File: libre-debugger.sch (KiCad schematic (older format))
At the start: 76 parts, among them J1 USB_C_Receptacle_USB2.0, J2 Conn_ST_STDC14, J4 Conn_01x10, Q1 2N7002, SW1 SW_SPDT, SW2 SW_Push, U1 FT2232H, U10 74LVC1G125, U11 74LVC1G125, U12 74LVC1G125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

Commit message: Progress placement.
Most components placed.
Most routing pending.
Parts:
- added LOGO1: Logo_Open_Hardware_Small, Symbol:OSHW-Logo_5.7x6mm_SilkScreen, symbol Graphic:Logo_Open_Hardware_Small
- J4: value Conn_01x10 -> Conn_01x14; footprint Connector_PinHeader_2.54mm:PinHeader_1x10_P2.54mm_Vertical -> Connector_PinHeader_2.54mm:PinHeader_1x14_P2.54mm_Vertical; symbol Connector_Generic:Conn_01x10 -> Connector_Generic:Conn_01x14
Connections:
- net labels added: GPIO0, GPIO1, GPIO2, GPIO3
- wire segments 338 -> 346
- no-connect marks 22 -> 18
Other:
- note added: "CAP on VREGIN?"
- moved on the sheet: D1, R7
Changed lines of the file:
@@
 EESchema Schematic File Version 5
-LIBS:libre-debugger-cache
 EELAYER 30 0
 EELAYER END
@@
 Comment3 ""
 Comment4 ""
+Comment5 ""
+Comment6 ""
+Comment7 ""
+Comment8 ""
+Comment9 ""
 $EndDescr
 Text Label 5650 5150 0    50   ~ 0
@@
 $EndComp
 $Comp
-L Graphic:Logo_Open_Hardware_Small #LOGO1
+L Graphic:Logo_Open_Hardware_Small LOGO1
 U 1 1 5C96BFCB
 P 15550 10250
-F 0 "#LOGO1" H 15550 10525 50  0001 C CNN
+F 0 "LOGO1" H 15550 10525 50  0001 C CNN
 F 1 "Logo_Open_Hardware_Small" H 15550 10025 50  0001 C CNN
-F 2 "" H 15550 10250 50  0001 C CNN
+F 2 "Symbol:OSHW-Logo_5.7x6mm_SilkScreen" H 15550 10250 50  0001 C CNN
 F 3 "~" H 15550 10250 50  0001 C CNN
 	1    15550 10250
@@
 L Device:LED D1
 U 1 1 5C62F385
-P 8900 5300
-F 0 "D1" V 8950 5150 50  0000 C CNN
-F 1 "LED" V 8850 5150 50  0000 C CNN
-F 2 "LED_SMD:LED_0603_1608Metric" H 8900 5300 50  0001 C CNN
-F 3 "~" H 8900 5300 50  0001 C CNN
-	1    8900 5300
+P 9200 5300
+F 0 "D1" V 9250 5150 50  0000 C CNN
+F 1 "LED" V 9150 5150 50  0000 C CNN
+F 2 "LED_SMD:LED_0603_1608Metric" H 9200 5300 50  0001 C CNN
+F 3 "~" H 9200 5300 50  0001 C CNN
+	1    9200 5300
 	0    -1   -1   0
 $EndComp
-Text Label 8900 5150 0    50   ~ 0
+Text Label 9200 5150 0    50   ~ 0
 MPSSE_LED_A
 Wire Wire Line
-	8400 4750 8900 4750
+	8400 4750 9200 4750
 $Comp
 L power:GND #PWR031
 U 1 1 5C6507DD
-P 8900 5500
-F 0 "#PWR031" H 8900 5250 50  0001 C CNN
-F 1 "GND" H 8905 5327 50  0000 C CNN
-F 2 "" H 8900 5500 50  0001 C CNN
-F 3 "" H 8900 5500 50  0001 C CNN
-	1    8900 5500
+P 9200 5500
+F 0 "#PWR031" H 9200 5250 50  0001 C CNN
+F 1 "GND" H 9205 5327 50  0000 C CNN
+F 2 "" H 9200 5500 50  0001 C CNN
+F 3 "" H 9200 5500 50  0001 C CNN
+	1    9200 5500
 	1    0    0    -1
 $EndComp
@@
 L Device:R R7
 U 1 1 5C62F38F
-P 8900 4900
-F 0 "R7" H 8800 4850 50  0000 C CNN
-F 1 "470R" H 8750 4950 50  0000 C CNN
-F 2 "Resistor_SMD:R_0603_1608Metric" V 8830 4900 50  0001 C CNN
-F 3 "~" H 8900 4900 50  0001 C CNN
-	1    8900 4900
+P 9200 4900
+F 0 "R7" H 9100 4850 50  0000 C CNN
+F 1 "470R" H 9050 4950 50  0000 C CNN
+F 2 "Resistor_SMD:R_0603_1608Metric" V 9130 4900 50  0001 C CNN
+F 3 "~" H 9200 4900 50  0001 C CNN
+	1    9200 4900
 	-1   0    0    1
 $EndComp
 Wire Wire Line
-	8900 5500 8900 5450
-Wire Wire Line
-	8900 5150 8900 5050
+	9200 5500 9200 5450
+Wire Wire Line
+	9200 5150 9200 5050
 Wire Wire Line
 	8400 4350 9950 4350
@@
 NoConn ~ 8400 5450
 NoConn ~ 8400 5350
-NoConn ~ 8400 5250
-NoConn ~ 8400 5150
-NoConn ~ 8400 5050
-NoConn ~ 8400 4950
 NoConn ~ 8400 7750
 $Comp
@@
 Text Label 5650 5350 0    50   ~ 0
 REF
-Wire Wire Line
-	15450 6400 14700 6400
-Wire Wire Line
-	15450 6600 14700 6600
-Wire Wire Line
-	14700 6500 15450 6500
-Wire Wire Line
-	14700 6700 15450 6700
-Wire Wire Line
-	14700 6300 15450 6300
 Text Label 14900 6400 0    50   ~ 0
 TCK_TRGT
@@
 L power:GND #PWR0105
 U 1 1 5CB1DC59
-P 15350 7050
-F 0 "#PWR0105" H 15350 6800 50  0001 C CNN
-F 1 "GND" H 15355 6877 50  0000 C CNN
-F 2 "" H 15350 7050 50  0001 C CNN
-F 3 "" H 15350 7050 50  0001 C CNN
-	1    15350 7050
-	1    0    0    -1
-$EndComp
-Wire Wire Line
-	15350 7050 15350 7000
-Wire Wire Line
-	15350 7000 15450 7000
-Wire Wire Line
-	15000 6200 15450 6200
-Wire Wire Line
-	15250 6100 15450 6100
+P 14850 7050
+F 0 "#PWR0105" H 14850 6800 50  0001 C CNN
+F 1 "GND" H 14855 6877 50  0000 C CNN
+F 2 "" H 14850 7050 50  0001 C CNN
+F 3 "" H 14850 7050 50  0001 C CNN
+	1    14850 7050
+	1    0    0    -1
+$EndComp
 Text Label 12750 1000 0    50   ~ 0
 SRST_N_R
@@
 Connection ~ 9150 3350
 $Comp
-L Connector_Generic:Conn_01x10 J4
-U 1 1 5D592546
-P 15650 6500
-F 0 "J4" H 15600 7000 50  0000 L CNN
-F 1 "Conn_01x10" H 15500 5900 50  0000 L CNN
-F 2 "Connector_PinHeader_2.54mm:PinHeader_1x10_P2.54mm_Vertical" H 15650 6500 50  0001 C CNN
-F 3 "~" H 15650 6500 50  0001 C CNN
-	1    15650 6500
-	1    0    0    -1
-$EndComp
-$Comp
 L Connector:Conn_ST_STDC14 J2
 U 1 1 5D5978D5
@@
 Wire Wire Line
 	15100 3600 14450 3600
-Wire Wire Line
-	15450 6800 14700 6800
-Wire Wire Line
-	15450 6900 14700 6900
 Text Label 14900 6800 0    50   ~ 0
 TXD_TRGT
@@
 	14500 5700 16000 5700
 Wire Notes Line
-	16000 5700 16000 7300
+	16000 5700 16000 7550
 Wire Notes Line
-	16000 7300 14500 7300
+	16000 7550 14500 7550
 Wire Notes Line
-	14500 7300 14500 5700
+	14500 7550 14500 5700
 Text Notes 14550 5800 0    50   ~ 10
 AUX header
@@
 	0    1    1    0
 $EndComp
+Text Notes 5150 4150 0    50   ~ 0
+CAP on VREGIN?
+Wire Wire Line
+	15450 6800 14700 6800
+Wire Wire Line
+	15450 6900 14700 6900
+$Comp
+L Connector_Generic:Conn_01x14 J4
+U 1 1 5D592546
+P 15650 6700
+F 0 "J4" H 15600 7200 50  0000 L CNN
+F 1 "Conn_01x14" H 15400 5900 50  0000 L CNN
+F 2 "Connector_PinHeader_2.54mm:PinHeader_1x14_P2.54mm_Vertical" H 15650 6700 50  0001 C CNN
+F 3 "~" H 15650 6700 50  0001 C CNN
+	1    15650 6700
+	1    0    0    -1
+$EndComp
+Wire Wire Line
+	15250 6100 15450 6100
+Wire Wire Line
+	15000 6200 15450 6200
+Wire Wire Line
+	14700 6300 15450 6300
+Wire Wire Line
+	14700 6700 15450 6700
+Wire Wire Line
+	14700 6500 15450 6500
+Wire Wire Line
+	15450 6400 14700 6400
+Wire Wire Line
+	15450 6600 14700 6600
+Wire Wire Line
+	14850 7000 14850 7050
+Wire Wire Line
+	14850 7000 15450 7000
+Text Label 8450 5250 0    50   ~ 0
+GPIO3
+Text Label 8450 5150 0    50   ~ 0
+GPIO2
+Text Label 8450 5050 0    50   ~ 0
+GPIO1
+Text Label 8450 4950 0    50   ~ 0
+GPIO0
+Wire Wire Line
+	8400 4950 8700 4950
+Wire Wire Line
+	8400 5050 8700 5050
+Wire Wire Line
+	8400 5150 8700 5150
+Wire Wire Line
+	8400 5250 8700 5250
+Text Label 15150 7100 0    50   ~ 0
+GPIO3
+Wire Wire Line
+	15450 7100 15100 7100
+Wire Wire Line
+	15450 7200 15100 7200
+Wire Wire Line
+	15450 7300 15100 7300
+Wire Wire Line
+	15450 7400 15100 7400
+Text Label 15150 7200 0    50   ~ 0
+GPIO2
+Text Label 15150 7300 0    50   ~ 0
+GPIO1
+Text Label 15150 7400 0    50   ~ 0
+GPIO0
 $EndSCHEMATC

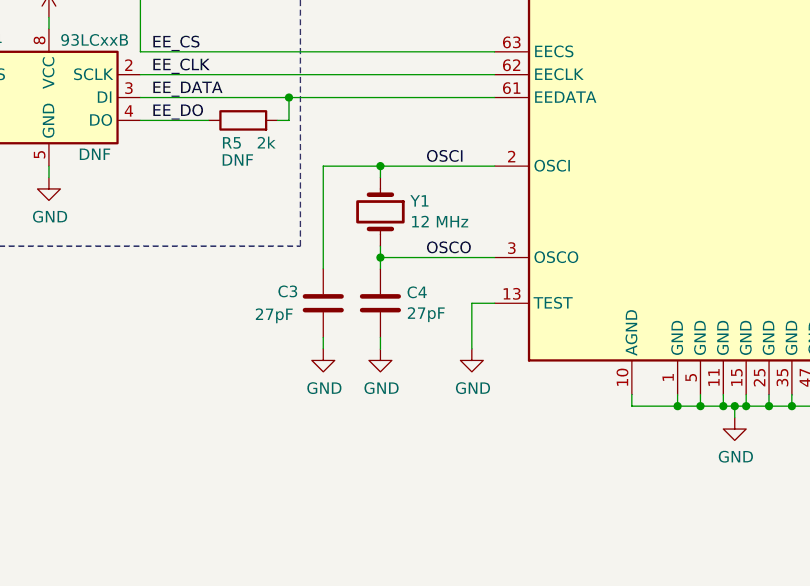
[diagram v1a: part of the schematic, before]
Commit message: SCH: Replace HC49 crystal by 3225
Schematic only. Layout update pending.
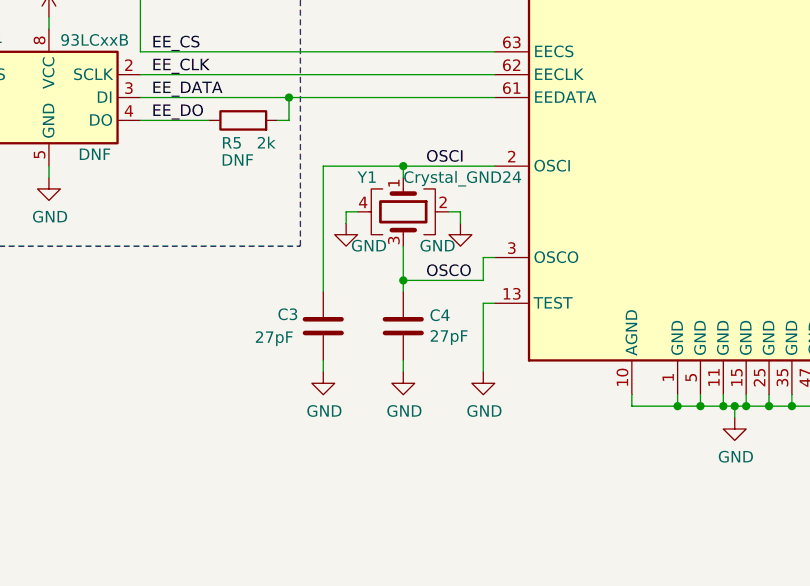
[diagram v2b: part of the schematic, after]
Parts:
- removed Y1: 12 MHz, Crystal:Crystal_SMD_HC49-SD, symbol Device:Crystal
- added Y1: Crystal_GND24, Crystal:Crystal_SMD_3225-4Pin_3.2x2.5mm, symbol Device:Crystal_GND24
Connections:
- wire segments 346 -> 352
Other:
- moved on the sheet: C3, C4
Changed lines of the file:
@@
 Text Label 5650 5050 0    50   ~ 0
 USB_DM
-$Comp
-L Device:Crystal Y1
-U 1 1 5C621971
-P 5500 7350
-F 0 "Y1" V 5454 7481 50  0000 L CNN
-F 1 "12 MHz" V 5545 7481 50  0000 L CNN
-F 2 "Crystal:Crystal_SMD_HC49-SD" H 5500 7350 50  0001 C CNN
-F 3 "~" H 5500 7350 50  0001 C CNN
-	1    5500 7350
-	0    1    1    0
-$EndComp
-Wire Wire Line
-	6000 7550 5500 7550
-Wire Wire Line
-	5500 7550 5500 7500
-Wire Wire Line
-	6000 7150 5500 7150
-Wire Wire Line
-	5500 7150 5500 7200
+Wire Wire Line
+	6000 7550 5950 7550
 $Comp
 L Device:C C4
 U 1 1 5C623C6B
-P 5500 7750
-F 0 "C4" H 5615 7796 50  0000 L CNN
-F 1 "27pF" H 5615 7705 50  0000 L CNN
-F 2 "Capacitor_SMD:C_0603_1608Metric" H 5538 7600 50  0001 C CNN
-F 3 "~" H 5500 7750 50  0001 C CNN
-	1    5500 7750
+P 5600 7850
+F 0 "C4" H 5715 7896 50  0000 L CNN
+F 1 "27pF" H 5715 7805 50  0000 L CNN
+F 2 "Capacitor_SMD:C_0603_1608Metric" H 5638 7700 50  0001 C CNN
+F 3 "~" H 5600 7850 50  0001 C CNN
+	1    5600 7850
 	1    0    0    -1
 $EndComp
@@
 L Device:C C3
 U 1 1 5C6244F4
-P 5250 7750
-F 0 "C3" H 5050 7800 50  0000 L CNN
-F 1 "27pF" H 4950 7700 50  0000 L CNN
-F 2 "Capacitor_SMD:C_0603_1608Metric" H 5288 7600 50  0001 C CNN
-F 3 "~" H 5250 7750 50  0001 C CNN
-	1    5250 7750
+P 5250 7850
+F 0 "C3" H 5050 7900 50  0000 L CNN
+F 1 "27pF" H 4950 7800 50  0000 L CNN
+F 2 "Capacitor_SMD:C_0603_1608Metric" H 5288 7700 50  0001 C CNN
+F 3 "~" H 5250 7850 50  0001 C CNN
+	1    5250 7850
 	1    0    0    -1
 $EndComp
@@
 L power:GND #PWR020
 U 1 1 5C624CB0
-P 5500 7950
-F 0 "#PWR020" H 5500 7700 50  0001 C CNN
-F 1 "GND" H 5505 7777 50  0000 C CNN
-F 2 "" H 5500 7950 50  0001 C CNN
-F 3 "" H 5500 7950 50  0001 C CNN
-	1    5500 7950
-	1    0    0    -1
-$EndComp
-Wire Wire Line
-	5500 7950 5500 7900
+P 5600 8050
+F 0 "#PWR020" H 5600 7800 50  0001 C CNN
+F 1 "GND" H 5605 7877 50  0000 C CNN
+F 2 "" H 5600 8050 50  0001 C CNN
+F 3 "" H 5600 8050 50  0001 C CNN
+	1    5600 8050
+	1    0    0    -1
+$EndComp
+Wire Wire Line
+	5600 8050 5600 8000
 $Comp
 L power:GND #PWR018
 U 1 1 5C625676
-P 5250 7950
-F 0 "#PWR018" H 5250 7700 50  0001 C CNN
-F 1 "GND" H 5255 7777 50  0000 C CNN
-F 2 "" H 5250 7950 50  0001 C CNN
-F 3 "" H 5250 7950 50  0001 C CNN
-	1    5250 7950
-	1    0    0    -1
-$EndComp
-Wire Wire Line
-	5250 7950 5250 7900
-Wire Wire Line
-	5500 7550 5500 7600
-Connection ~ 5500 7550
-Wire Wire Line
-	5250 7600 5250 7150
-Wire Wire Line
-	5250 7150 5500 7150
-Connection ~ 5500 7150
+P 5250 8050
+F 0 "#PWR018" H 5250 7800 50  0001 C CNN
+F 1 "GND" H 5255 7877 50  0000 C CNN
+F 2 "" H 5250 8050 50  0001 C CNN
+F 3 "" H 5250 8050 50  0001 C CNN
+	1    5250 8050
+	1    0    0    -1
+$EndComp
+Wire Wire Line
+	5250 8050 5250 8000
+Wire Wire Line
+	5250 7700 5250 7150
 $Comp
 L power:GND #PWR025
 U 1 1 5C62824D
-P 5900 7950
-F 0 "#PWR025" H 5900 7700 50  0001 C CNN
-F 1 "GND" H 5905 7777 50  0000 C CNN
-F 2 "" H 5900 7950 50  0001 C CNN
-F 3 "" H 5900 7950 50  0001 C CNN
-	1    5900 7950
-	1    0    0    -1
-$EndComp
-Wire Wire Line
-	5900 7950 5900 7750
-Wire Wire Line
-	5900 7750 6000 7750
+P 5950 8050
+F 0 "#PWR025" H 5950 7800 50  0001 C CNN
+F 1 "GND" H 5955 7877 50  0000 C CNN
+F 2 "" H 5950 8050 50  0001 C CNN
+F 3 "" H 5950 8050 50  0001 C CNN
+	1    5950 8050
+	1    0    0    -1
+$EndComp
+Wire Wire Line
+	5950 8050 5950 7750
+Wire Wire Line
+	5950 7750 6000 7750
 $Comp
 L Memory_EEPROM:93LCxxB U4
@@
 Text Label 5700 7150 0    50   ~ 0
 OSCI
-Text Label 5700 7550 0    50   ~ 0
+Text Label 5700 7650 0    50   ~ 0
 OSCO
 $Comp
@@
 Text Label 15150 7400 0    50   ~ 0
 GPIO0
+$Comp
+L Device:Crystal_GND24 Y1
+U 1 1 5D9E4D58
+P 5600 7350
+F 0 "Y1" V 5450 7150 50  0000 L CNN
+F 1 "Crystal_GND24" V 5450 7350 50  0000 L CNN
+F 2 "Crystal:Crystal_SMD_3225-4Pin_3.2x2.5mm" H 5600 7350 50  0001 C CNN
+F 3 "~" H 5600 7350 50  0001 C CNN
+	1    5600 7350
+	0    1    1    0
+$EndComp
+Wire Wire Line
+	5250 7150 5600 7150
+Wire Wire Line
+	5600 7200 5600 7150
+Connection ~ 5600 7150
+Wire Wire Line
+	5600 7150 6000 7150
+$Comp
+L power:GND #PWR?
+U 1 1 5D9EB372
+P 5850 7400
+F 0 "#PWR?" H 5850 7150 50  0001 C CNN
+F 1 "GND" H 5750 7300 50  0000 C CNN
+F 2 "" H 5850 7400 50  0001 C CNN
+F 3 "" H 5850 7400 50  0001 C CNN
+	1    5850 7400
+	1    0    0    -1
+$EndComp
+$Comp
+L power:GND #PWR?
+U 1 1 5D9EBAF5
+P 5350 7400
+F 0 "#PWR?" H 5350 7150 50  0001 C CNN
+F 1 "GND" H 5450 7300 50  0000 C CNN
+F 2 "" H 5350 7400 50  0001 C CNN
+F 3 "" H 5350 7400 50  0001 C CNN
+	1    5350 7400
+	1    0    0    -1
+$EndComp
+Wire Wire Line
+	5350 7400 5350 7350
+Wire Wire Line
+	5350 7350 5400 7350
+Wire Wire Line
+	5850 7400 5850 7350
+Wire Wire Line
+	5850 7350 5800 7350
+Wire Wire Line
+	5950 7550 5950 7650
+Wire Wire Line
+	5600 7650 5950 7650
+Connection ~ 5600 7650
+Wire Wire Line
+	5600 7650 5600 7700
+Wire Wire Line
+	5600 7500 5600 7650
 $EndSCHEMATC

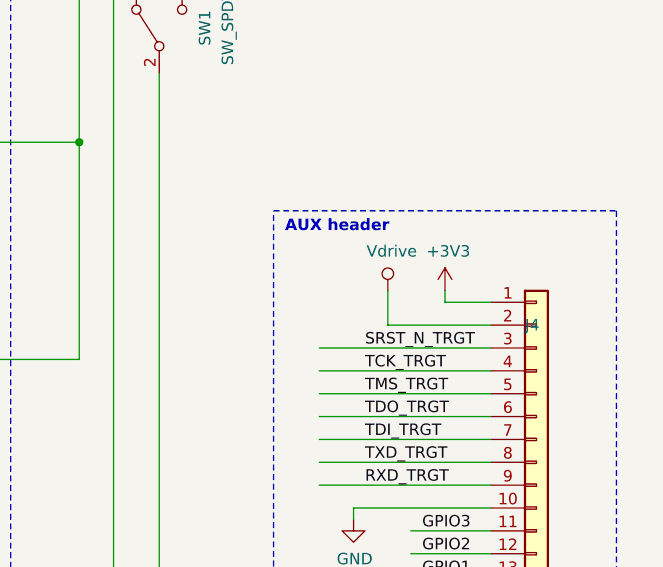
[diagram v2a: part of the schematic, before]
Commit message: SCH: V_Drive_R for the 2.54mm header too
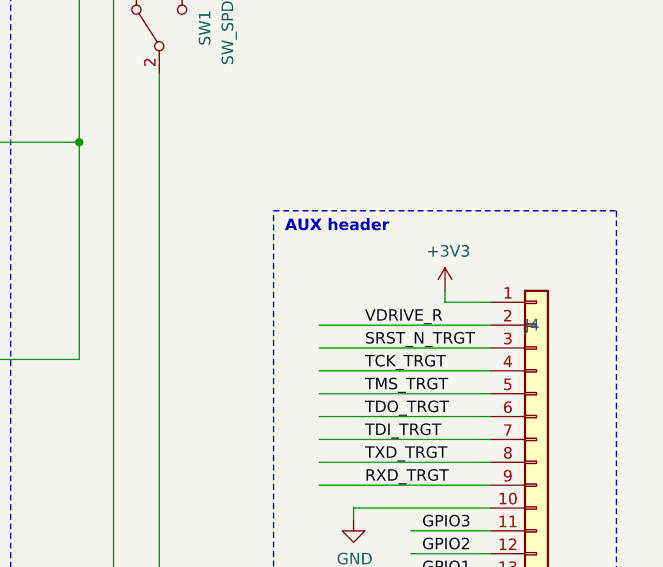
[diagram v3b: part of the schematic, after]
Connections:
- wire segments 352 -> 351
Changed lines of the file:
@@
 SRST_N_TRGT
-$Comp
-L power:Vdrive #PWR0103
-U 1 1 5CB1B331
-P 15000 6050
-F 0 "#PWR0103" H 14800 5900 50  0001 C CNN
-F 1 "Vdrive" H 15017 6223 50  0000 C CNN
-F 2 "" H 15000 6050 50  0001 C CNN
-F 3 "" H 15000 6050 50  0001 C CNN
-	1    15000 6050
-	1    0    0    -1
-$EndComp
-Wire Wire Line
-	15000 6050 15000 6200
 $Comp
 L power:+3V3 #PWR0104
@@
 	15250 6100 15450 6100
 Wire Wire Line
-	15000 6200 15450 6200
-Wire Wire Line
 	14700 6300 15450 6300
 Wire Wire Line
@@
 	5600 7150 6000 7150
 $Comp
-L power:GND #PWR?
+L power:GND #PWR0103
 U 1 1 5D9EB372
 P 5850 7400
-F 0 "#PWR?" H 5850 7150 50  0001 C CNN
+F 0 "#PWR0103" H 5850 7150 50  0001 C CNN
 F 1 "GND" H 5750 7300 50  0000 C CNN
 F 2 "" H 5850 7400 50  0001 C CNN
@@
 $EndComp
 $Comp
-L power:GND #PWR?
+L power:GND #PWR0107
 U 1 1 5D9EBAF5
 P 5350 7400
-F 0 "#PWR?" H 5350 7150 50  0001 C CNN
+F 0 "#PWR0107" H 5350 7150 50  0001 C CNN
 F 1 "GND" H 5450 7300 50  0000 C CNN
 F 2 "" H 5350 7400 50  0001 C CNN
@@
 Wire Wire Line
 	5600 7500 5600 7650
+Wire Wire Line
+	14700 6200 15450 6200
+Text Label 14900 6200 0    50   ~ 0
+VDRIVE_R
 $EndSCHEMATC

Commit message: A few SCH changes:
- add extra decoupling caps on V_DRIVE
- Name net SWD_EN_LED
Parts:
- added C19, C20, C21: 100nF, Capacitor_SMD:C_0603_1608Metric, symbol Device:C
- J4: value Conn_01x14 -> Conn_01x16; footprint Connector_PinHeader_2.54mm:PinHeader_1x14_P2.54mm_Vertical -> Connector_PinHeader_2.54mm:PinHeader_1x16_P2.54mm_Vertical; symbol Connector_Generic:Conn_01x14 -> Connector_Generic:Conn_01x16
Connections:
- net labels added: SWD_EN_LED
- wire segments 351 -> 365
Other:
- moved on the sheet: D6, R17

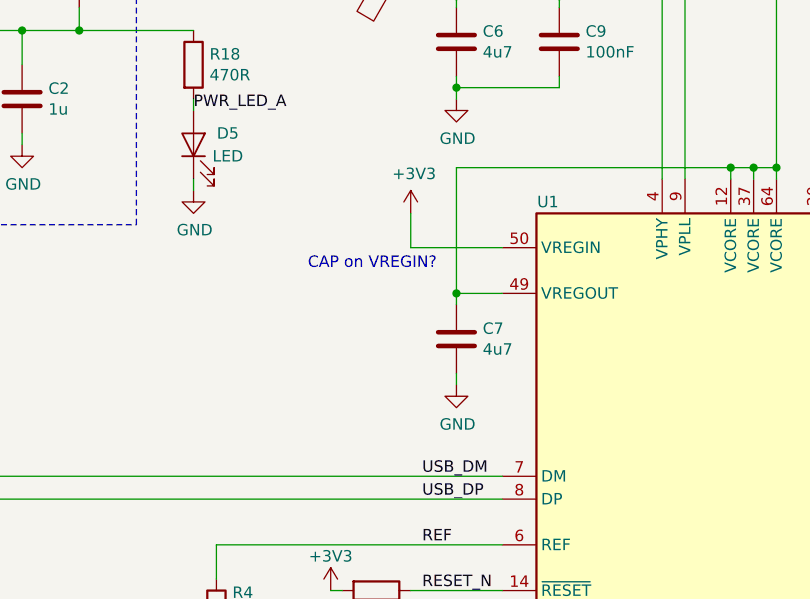
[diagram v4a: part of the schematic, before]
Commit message: SCH: add cap on VREGIN
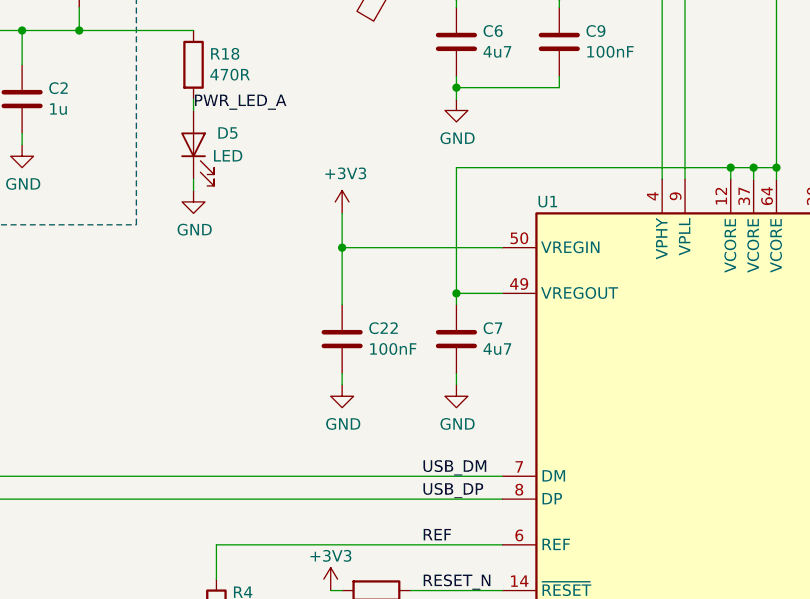
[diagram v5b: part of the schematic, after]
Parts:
- added C22: 100nF, Capacitor_SMD:C_0603_1608Metric, symbol Device:C
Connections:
- wire segments 365 -> 367
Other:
- note removed: "CAP on VREGIN?"
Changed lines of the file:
@@
 L power:+3V3 #PWR021
 U 1 1 5C67B7F7
-P 5600 3900
-F 0 "#PWR021" H 5600 3750 50  0001 C CNN
-F 1 "+3V3" H 5615 4073 50  0000 C CNN
-F 2 "" H 5600 3900 50  0001 C CNN
-F 3 "" H 5600 3900 50  0001 C CNN
-	1    5600 3900
-	1    0    0    -1
-$EndComp
-Wire Wire Line
-	6000 4050 5600 4050
-Wire Wire Line
-	5600 4050 5600 3900
+P 5300 3900
+F 0 "#PWR021" H 5300 3750 50  0001 C CNN
+F 1 "+3V3" H 5315 4073 50  0000 C CNN
+F 2 "" H 5300 3900 50  0001 C CNN
+F 3 "" H 5300 3900 50  0001 C CNN
+	1    5300 3900
+	1    0    0    -1
+$EndComp
+Wire Wire Line
+	6000 4050 5300 4050
+Wire Wire Line
+	5300 4050 5300 3900
 Wire Wire Line
 	4450 6650 4450 6250
@@
 Wire Wire Line
 	8400 4650 10600 4650
-$Comp
-L Interface_USB:FT2232H U1
-U 1 1 5C60DA40
-P 7200 5950
-F 0 "U1" H 6200 8050 50  0000 C CNN
-F 1 "FT2232H" H 8100 8050 50  0000 C CNN
-F 2 "Package_QFP:LQFP-64_10x10mm_P0.5mm" H 7200 5950 50  0001 C CNN
-F 3 "http://www.ftdichip.com/Products/ICs/FT2232H.html" H 7200 5950 50  0001 C CNN
-F 4 "FTDI" H 7200 5950 50  0001 C CNN "Manufacturer"
-F 5 "FT2232HL" H 7200 5950 50  0001 C CNN "MPN"
-	1    7200 5950
-	1    0    0    -1
-$EndComp
 NoConn ~ 8400 7450
 NoConn ~ 8400 7350
@@
 	0    1    1    0
 $EndComp
-Text Notes 5150 4150 0    50   ~ 0
-CAP on VREGIN?
 Wire Wire Line
 	15450 7000 14700 7000
@@
 	1    0    0    -1
 $EndComp
+$Comp
+L Interface_USB:FT2232H U1
+U 1 1 5C60DA40
+P 7200 5950
+F 0 "U1" H 6200 8050 50  0000 C CNN
+F 1 "FT2232H" H 8100 8050 50  0000 C CNN
+F 2 "Package_QFP:LQFP-64_10x10mm_P0.5mm" H 7200 5950 50  0001 C CNN
+F 3 "http://www.ftdichip.com/Products/ICs/FT2232H.html" H 7200 5950 50  0001 C CNN
+F 4 "FTDI" H 7200 5950 50  0001 C CNN "Manufacturer"
+F 5 "FT2232HL" H 7200 5950 50  0001 C CNN "MPN"
+	1    7200 5950
+	1    0    0    -1
+$EndComp
+$Comp
+L Device:C C22
+U 1 1 5DB8298F
+P 5300 4450
+F 0 "C22" H 5415 4496 50  0000 L CNN
+F 1 "100nF" H 5415 4405 50  0000 L CNN
+F 2 "Capacitor_SMD:C_0603_1608Metric" H 5338 4300 50  0001 C CNN
+F 3 "~" H 5300 4450 50  0001 C CNN
+	1    5300 4450
+	1    0    0    -1
+$EndComp
+Wire Wire Line
+	5300 4300 5300 4050
+Connection ~ 5300 4050
+$Comp
+L power:GND #PWR064
+U 1 1 5DB83C82
+P 5300 4650
+F 0 "#PWR064" H 5300 4400 50  0001 C CNN
+F 1 "GND" H 5305 4477 50  0000 C CNN
+F 2 "" H 5300 4650 50  0001 C CNN
+F 3 "" H 5300 4650 50  0001 C CNN
+	1    5300 4650
+	1    0    0    -1
+$EndComp
+Wire Wire Line
+	5300 4650 5300 4600
 $EndSCHEMATC
